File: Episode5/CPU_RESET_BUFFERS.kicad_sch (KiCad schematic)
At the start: 16 parts, among them J2 SLOT, U1 74HCT541, U13 74HCT244, U2 74HCT245, U3 74HCT541

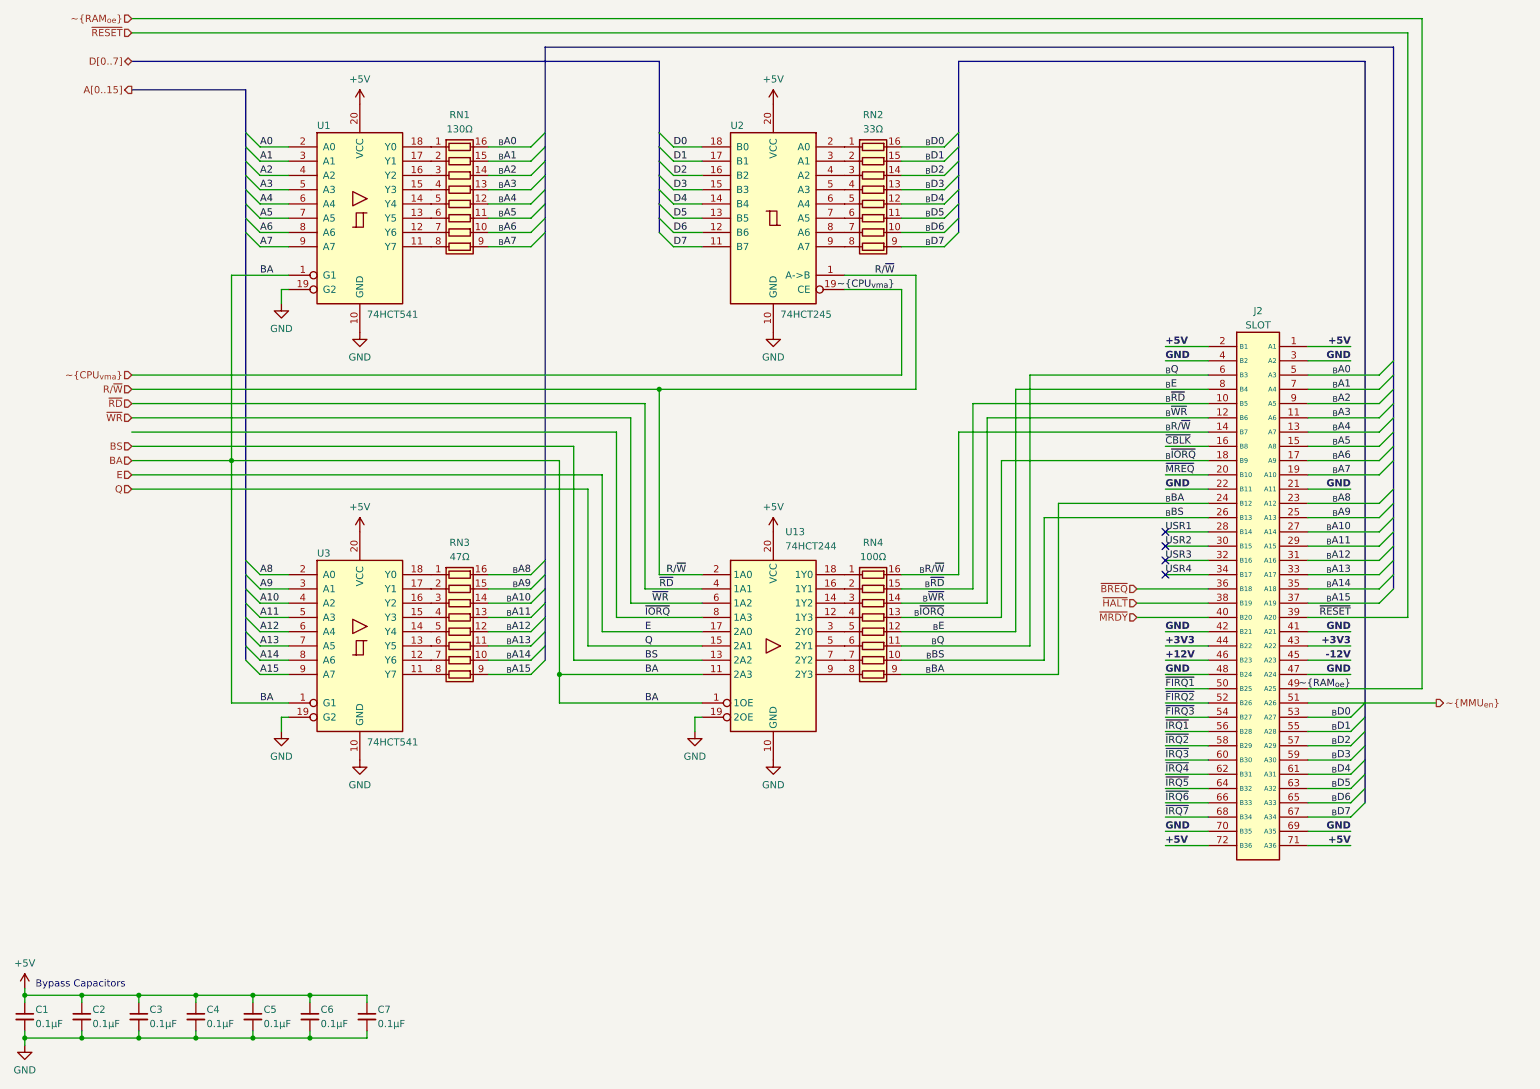
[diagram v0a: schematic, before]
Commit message: Placed Global labels instead. And toying with new PLDs
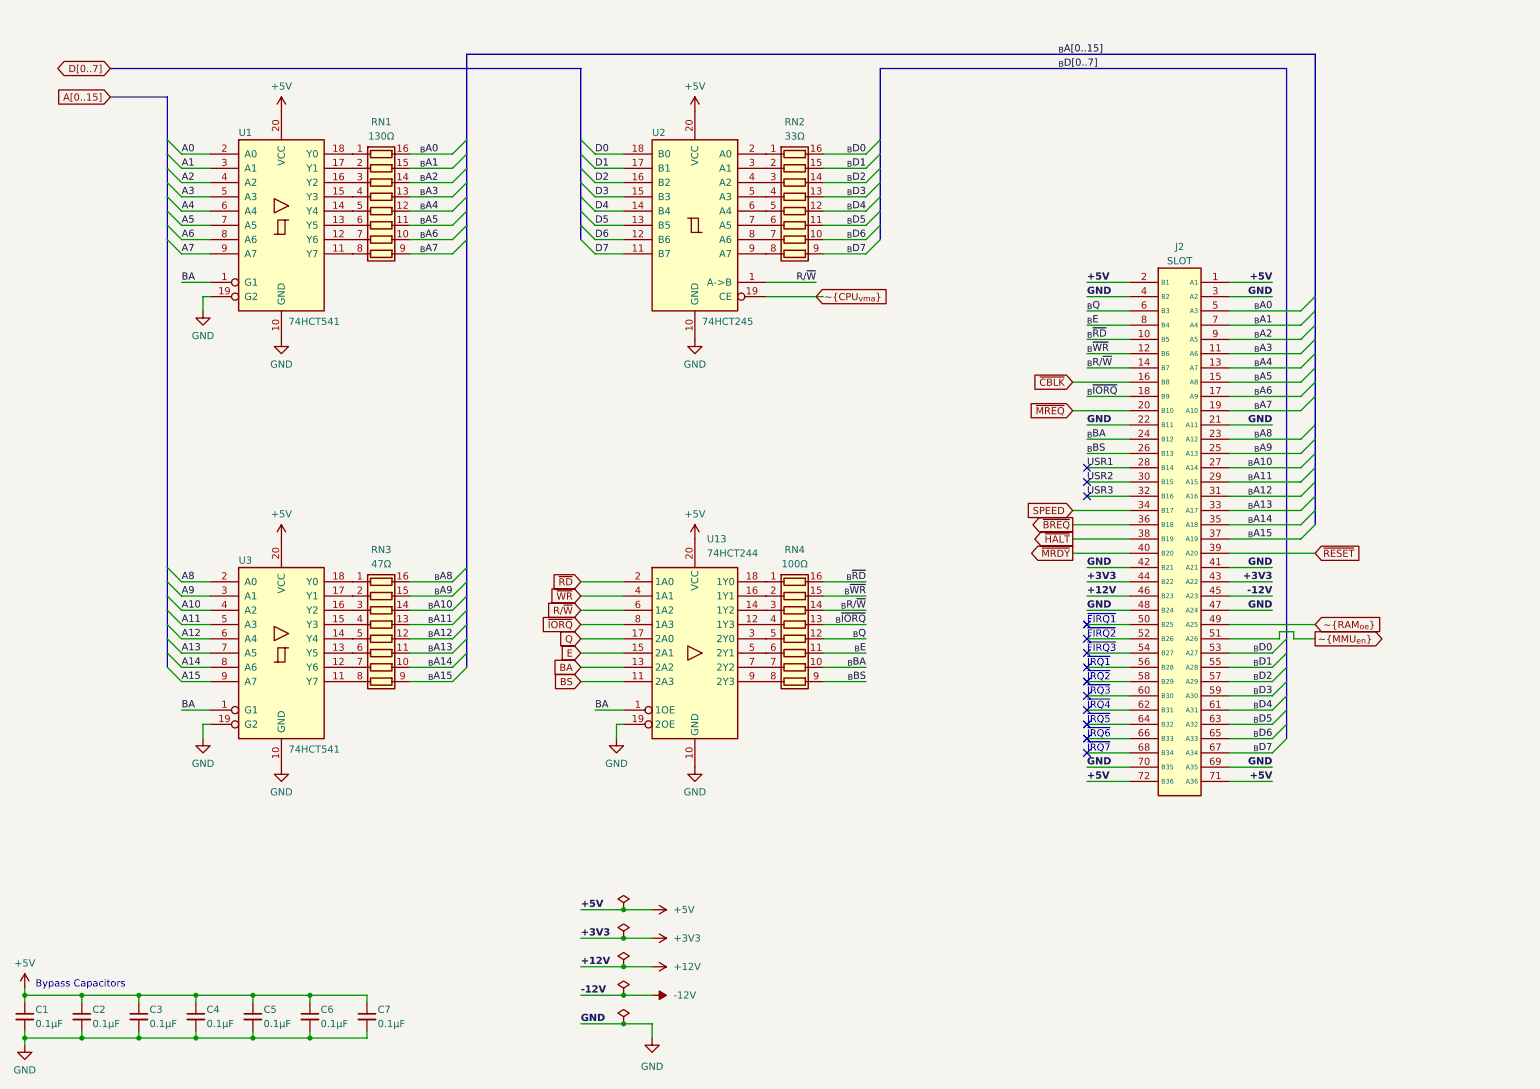
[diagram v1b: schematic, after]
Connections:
- net BA: now also U13.13 (2A2); no longer U13.11 (2A3)
- net BS: now also U13.11 (2A3); no longer U13.13 (2A2)
- net E: now also U13.15 (2A1); no longer U13.17 (2A0)
- net Q: now also U13.17 (2A0); no longer U13.15 (2A1)
- net R/~{W}: now also U13.6 (1A2); no longer U13.2 (1A0)
- net _{B}BA: now also RN4.10 (R7.2); no longer RN4.9 (R8.2)
- net _{B}BS: now also RN4.9 (R8.2); no longer RN4.10 (R7.2)
- net _{B}E: now also RN4.11 (R6.2); no longer RN4.12 (R5.2)
- net _{B}Q: now also RN4.12 (R5.2); no longer RN4.11 (R6.2)
- net _{B}R/~{W}: now also RN4.14 (R3.2); no longer RN4.16 (R1.2)
- net _{B}~{RD}: now also RN4.16 (R1.2); no longer RN4.15 (R2.2)
- net _{B}~{WR}: now also RN4.15 (R2.2); no longer RN4.14 (R3.2)
- net ~{RD}: now also U13.2 (1A0); no longer U13.4 (1A1)
- net ~{WR}: now also U13.4 (1A1); no longer U13.6 (1A2)
- net USR4 renamed SPEED
- net ~{FIRQ1}: no longer names the net of J2.50 (B25)
- net ~{FIRQ2}: no longer names the net of J2.52 (B26)
- net ~{FIRQ3}: no longer names the net of J2.54 (B27)
- net ~{IRQ1}: no longer names the net of J2.56 (B28)
- net ~{IRQ2}: no longer names the net of J2.58 (B29)
- net ~{IRQ3}: no longer names the net of J2.60 (B30)
- net ~{IRQ4}: no longer names the net of J2.62 (B31)
- net ~{IRQ5}: no longer names the net of J2.64 (B32)
- net ~{IRQ6}: no longer names the net of J2.66 (B33)
- net ~{IRQ7}: no longer names the net of J2.68 (B34)
- no-connect marks 4 -> 13
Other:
- note added: "~{FIRQ1}"
- note added: "~{FIRQ2}"
- note added: "~{FIRQ3}"
- note added: "~{IRQ1}"
- note added: "~{IRQ2}"
- note added: "~{IRQ3}"
- note added: "~{IRQ4}"
- note added: "~{IRQ5}"
- note added: "~{IRQ6}"
- note added: "~{IRQ7}"
- moved on the sheet: J2, RN1, RN2, RN3, RN4, U1, U13, U2, U3

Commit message: Toying with different alternatives for the CPU board
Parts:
- renumbered C5 to C10, C6 to C11, C7 to C12, C1 to C6, C2 to C7, C3 to C8, C4 to C9, J2 to J1, U1 to U5, U2 to U6, U3 to U7, U13 to U8
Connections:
- net ~{CPU_{vma}} is gone; now on net BA: U6.19 (CE)
- net ~{FIRQ}1: now reaches J1.50 (B25)
- net ~{FIRQ}2: now reaches J1.52 (B26)
- net ~{FIRQ}3: now reaches J1.54 (B27)
- net ~{IRQ}1: now reaches J1.56 (B28)
- net ~{IRQ}2: now reaches J1.58 (B29)
- net ~{IRQ}3: now reaches J1.60 (B30)
- net ~{IRQ}4: now reaches J1.62 (B31)
- net ~{IRQ}5: now reaches J1.64 (B32)
- net ~{IRQ}6: now reaches J1.66 (B33)
- net ~{IRQ}7: now reaches J1.68 (B34)
- net SPEED renamed USR4
- no-connect marks 13 -> 4
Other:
- note removed: "~{FIRQ1}"
- note removed: "~{FIRQ2}"
- note removed: "~{FIRQ3}"
- note removed: "~{IRQ1}"
- note removed: "~{IRQ2}"
- note removed: "~{IRQ3}"
- note removed: "~{IRQ4}"
- note removed: "~{IRQ5}"
- note removed: "~{IRQ6}"
- note removed: "~{IRQ7}"

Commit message: Finished the preliminary design of the CPU card
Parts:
- removed J1: SLOT, MicroHobbyist:72-pin CE connector, symbol MicroHobbyist:72-pin Card Edge (ISA style)
- removed RN4: 100Ω, Package_DIP:DIP-16_W7.62mm, symbol Device:R_Pack08
- added D1: RESET, symbol Device:LED
- added R1, R2, R3, R4, R5, R6, R7: 4K7Ω, symbol Device:R_Small_US
- added R10, R9: 47Ω, symbol Device:R_Small_US
- added R11, R12, R8: 33Ω, symbol Device:R_Small_US
- added R13: 220Ω, symbol Device:R_Small_US
- added SW1: RESET, symbol Switch:SW_Push
- added U3: HD63C09P, Package_DIP:DIP-40_W15.24mm_Socket, symbol CPU_NXP_6800:MC6809
- added U6: MIC1232, Package_DIP:DIP-8_W7.62mm_Socket, symbol MicroHobbyist:MIC1232
- RN1: value 130Ω -> 47Ω
- RN2: value 33Ω -> 22Ω
- RN3: value 47Ω -> 33Ω
- U1: renamed from U5; value 74HCT541 -> 74AHCT541
- U2: renamed from U6; value 74HCT245 -> 74AHCT245
- U4: renamed from U7; value 74HCT541 -> 74AHCT541
- U5: renamed from U8; value 74HCT244 -> 74AHCT244
- renumbered C6 to C1, C7 to C2, C8 to C3, C9 to C4, C10 to C5, C11 to C6, C12 to C7
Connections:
- net _{B}A0 is gone; now on net A0: RN1.16 (R1.2)
- net _{B}A1 is gone; now on net A1: RN1.15 (R2.2)
- net _{B}A10 is gone; now on net A10: RN3.14 (R3.2)
- net _{B}A11 is gone; now on net A11: RN3.13 (R4.2)
- net _{B}A12 is gone; now on net A12: RN3.12 (R5.2)
- net _{B}A13 is gone; now on net A13: RN3.11 (R6.2)
- net _{B}A14 is gone; now on net A14: RN3.10 (R7.2)
- net _{B}A15 is gone; now on net A15: RN3.9 (R8.2)
- net _{B}A2 is gone; now on net A2: RN1.14 (R3.2)
- net _{B}A3 is gone; now on net A3: RN1.13 (R4.2)
- net _{B}A4 is gone; now on net A4: RN1.12 (R5.2)
- net _{B}A5 is gone; now on net A5: RN1.11 (R6.2)
- net _{B}A6 is gone; now on net A6: RN1.10 (R7.2)
- net _{B}A7 is gone; now on net A7: RN1.9 (R8.2)
- net _{B}A8 is gone; now on net A8: RN3.16 (R1.2)
- net _{B}A9 is gone; now on net A9: RN3.15 (R2.2)
- net _{B}D0 is gone; now on net D0: RN2.16 (R1.2)
- net _{B}D1 is gone; now on net D1: RN2.15 (R2.2)
- net _{B}D2 is gone; now on net D2: RN2.14 (R3.2)
- net _{B}D3 is gone; now on net D3: RN2.13 (R4.2)
- net _{B}D4 is gone; now on net D4: RN2.12 (R5.2)
- net _{B}D5 is gone; now on net D5: RN2.11 (R6.2)
- net _{B}D6 is gone; now on net D6: RN2.10 (R7.2)
- net _{B}D7 is gone; now on net D7: RN2.9 (R8.2)
- net ~{IORQ} is gone; now on net GND: U5.8 (1A3)
- net ~{WR} is gone; now on net GND: U5.4 (1A1)
- net +5V: now also R1.2, R2.2, R3.2, R4.2, R5.2, R6.2, R7.2, U3.7 (VCC), U6.8 (VCC)
- net A0: no longer U1.2 (A0)
- net A1: no longer U1.3 (A1)
- net A10: no longer U4.4 (A2)
- net A11: no longer U4.5 (A3)
- net A12: no longer U4.6 (A4)
- net A13: no longer U4.7 (A5)
- net A14: no longer U4.8 (A6)
- net A15: no longer U4.9 (A7)
- net A2: no longer U1.4 (A2)
- net A3: no longer U1.5 (A3)
- net A4: no longer U1.6 (A4)
- net A5: no longer U1.7 (A5)
- net A6: no longer U1.8 (A6)
- net A7: no longer U1.9 (A7)
- net A8: no longer U4.2 (A0)
- net A9: no longer U4.3 (A1)
- net BA: now also R11.2; no longer U1.1 (G1), U2.19 (CE), U4.1 (G1), U5.1 (1OE), U5.13 (2A2)
- net BS: now also R12.2; no longer U5.11 (2A3)
- net D0: no longer U2.18 (B0)
- net D1: no longer U2.17 (B1)
- net D2: no longer U2.16 (B2)
- net D3: no longer U2.15 (B3)
- net D4: no longer U2.14 (B4)
- net D5: no longer U2.13 (B5)
- net D6: no longer U2.12 (B6)
- net D7: no longer U2.11 (B7)
- net E: now also R9.2; no longer U5.15 (2A1)
- net GND: now also U5.6 (1A2), D1.1 (K), SW1.1, U3.1 (VSS), U6.3 (TOL), U6.4 (GND)
- net Q: now also R10.2; no longer U5.17 (2A0)
- net R/~{W}: now also R8.2; no longer U5.6 (1A2)
- net ~{BREQ}: now also R6.1, U3.33 (~{DMA/BREQ})
- net ~{HALT}: now also R5.1, U3.40 (~{HALT})
- net ~{MRDY}: now also R4.1, U3.36 (MRDY)
- net ~{RESET}: now also R7.1, U3.37 (~{RESET}), U6.6 (~{RST})
- net at U5.18 (1Y0): now also R8.1
- net at U5.3 (2Y0): now also R9.1
- net at U5.5 (2Y1): now also R10.1
- net at U5.7 (2Y2): now also R11.1
- net at U5.9 (2Y3): now also R12.1
- net ~{RD} renamed _{ub}R/~{W}
- net _{ub}R/~{W}: now also U3.32 (R/~{W})
- new net: SW1.2, U6.1 (~{PBRST})
- new net: R13.2, U6.5 (RST)
- new net: D1.2 (A), R13.1
- new net AA0: U1.2 (A0), U3.8 (A0)
- new net AA1: U1.3 (A1), U3.9 (A1)
- new net AA10: U3.18 (A10), U4.4 (A2)
- new net AA11: U3.19 (A11), U4.5 (A3)
- new net AA12: U3.20 (A12), U4.6 (A4)
- new net AA13: U3.21 (A13), U4.7 (A5)
- new net AA14: U3.22 (A14), U4.8 (A6)
- new net AA15: U3.23 (A15), U4.9 (A7)
- new net AA2: U1.4 (A2), U3.10 (A2)
- new net AA3: U1.5 (A3), U3.11 (A3)
- new net AA4: U1.6 (A4), U3.12 (A4)
- new net AA5: U1.7 (A5), U3.13 (A5)
- new net AA6: U1.8 (A6), U3.14 (A6)
- new net AA7: U1.9 (A7), U3.15 (A7)
- new net AA8: U3.16 (A8), U4.2 (A0)
- new net AA9: U3.17 (A9), U4.3 (A1)
- new net CLK_{cpu}: U3.38 (EXTAL)
- new net DD0: U2.18 (B0), U3.31 (D0)
- new net DD1: U2.17 (B1), U3.30 (D1)
- new net DD2: U2.16 (B2), U3.29 (D2)
- new net DD3: U2.15 (B3), U3.28 (D3)
- new net DD4: U2.14 (B4), U3.27 (D4)
- new net DD5: U2.13 (B5), U3.26 (D5)
- new net DD6: U2.12 (B6), U3.25 (D6)
- new net DD7: U2.11 (B7), U3.24 (D7)
- new net _{ub}BA: U1.1 (G1), U2.19 (CE), U3.6 (BA), U4.1 (G1), U5.1 (1OE), U5.13 (2A2)
- new net _{ub}BS: U3.5 (BS), U5.11 (2A3)
- new net _{ub}E: U3.34 (E), U5.17 (2A0)
- new net _{ub}Q: U3.35 (Q), U5.15 (2A1), U6.7 (~{ST})
- new net ~{FIRQ}: R3.1, U3.4 (~{FIRQ})
- new net ~{IRQ}: R2.1, U3.3 (~{IRQ})
- new net ~{NMI}: R1.1, U3.2 (~{NMI})
- no-connect marks 4 -> 5
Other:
- company: Frédéric "MicroHobbyist" Segard -> MicroHobbyist
- title: (none) -> CPU, Clock, Reset, and Buffers
- moved on the sheet: RN1, RN2, RN3, U1, U2, U4, U5
